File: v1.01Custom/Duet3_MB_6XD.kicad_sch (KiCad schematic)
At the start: 0 parts

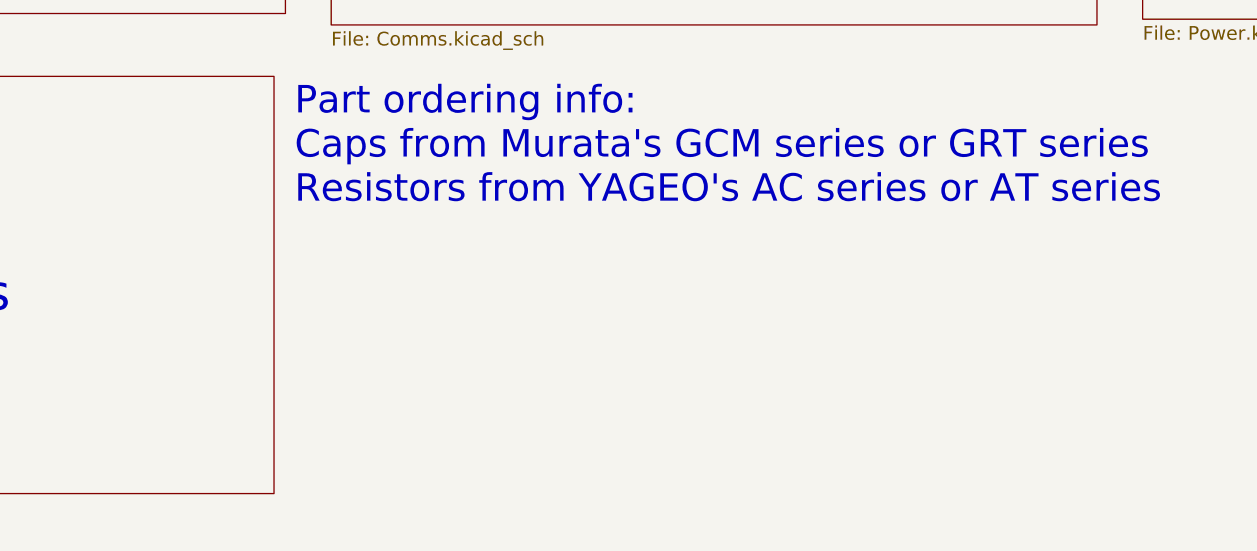
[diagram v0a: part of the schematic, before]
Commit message: Update Duet3_MB_6XD.kicad_sch
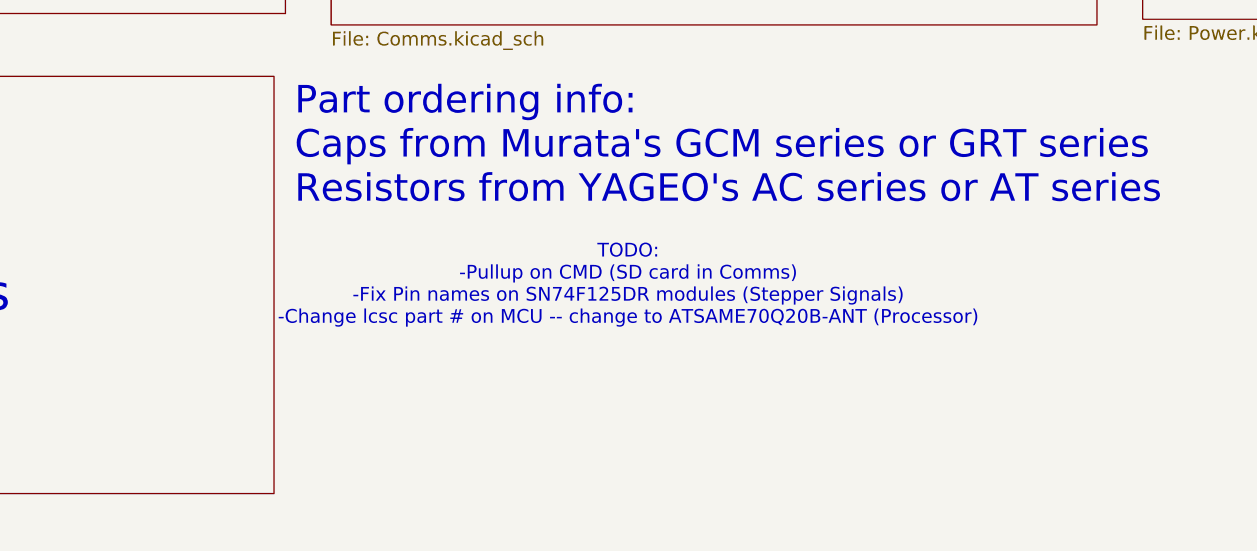
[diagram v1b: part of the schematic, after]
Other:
- note added: "TODO: -Pullup on CMD (SD card in Comms) -Fix Pin names on SN74F125DR modules (Stepper Signals) -Change lcsc part # on MCU -- change to ATSAME70Q20B-ANT (Processor)"
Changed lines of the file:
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@@
 		(comment 1 "(c) Duet3D")
+	)
+	(text "TODO:\n-Pullup on CMD (SD card in Comms)\n-Fix Pin names on SN74F125DR modules (Stepper Signals)\n-Change lcsc part # on MCU -- change to ATSAME70Q20B-ANT (Processor)"
+		(exclude_from_sim no)
+		(at 138.43 168.656 0)
+		(effects
+			(font
+				(size 1.524 1.524)
+			)
+		)
 	)
 	(text "Duet3 Mainboard 6XD"
